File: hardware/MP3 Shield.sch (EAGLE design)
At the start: 62 parts, among them J1 ISP/SPI, Q1 12.288MHz, U1 3.3V, U2 ARDUINO_R3_SHIELD, U3 VS1053, U4 1.8V, U6 USD-SOCKET, U7 74HC4050 LVL CONVERTER

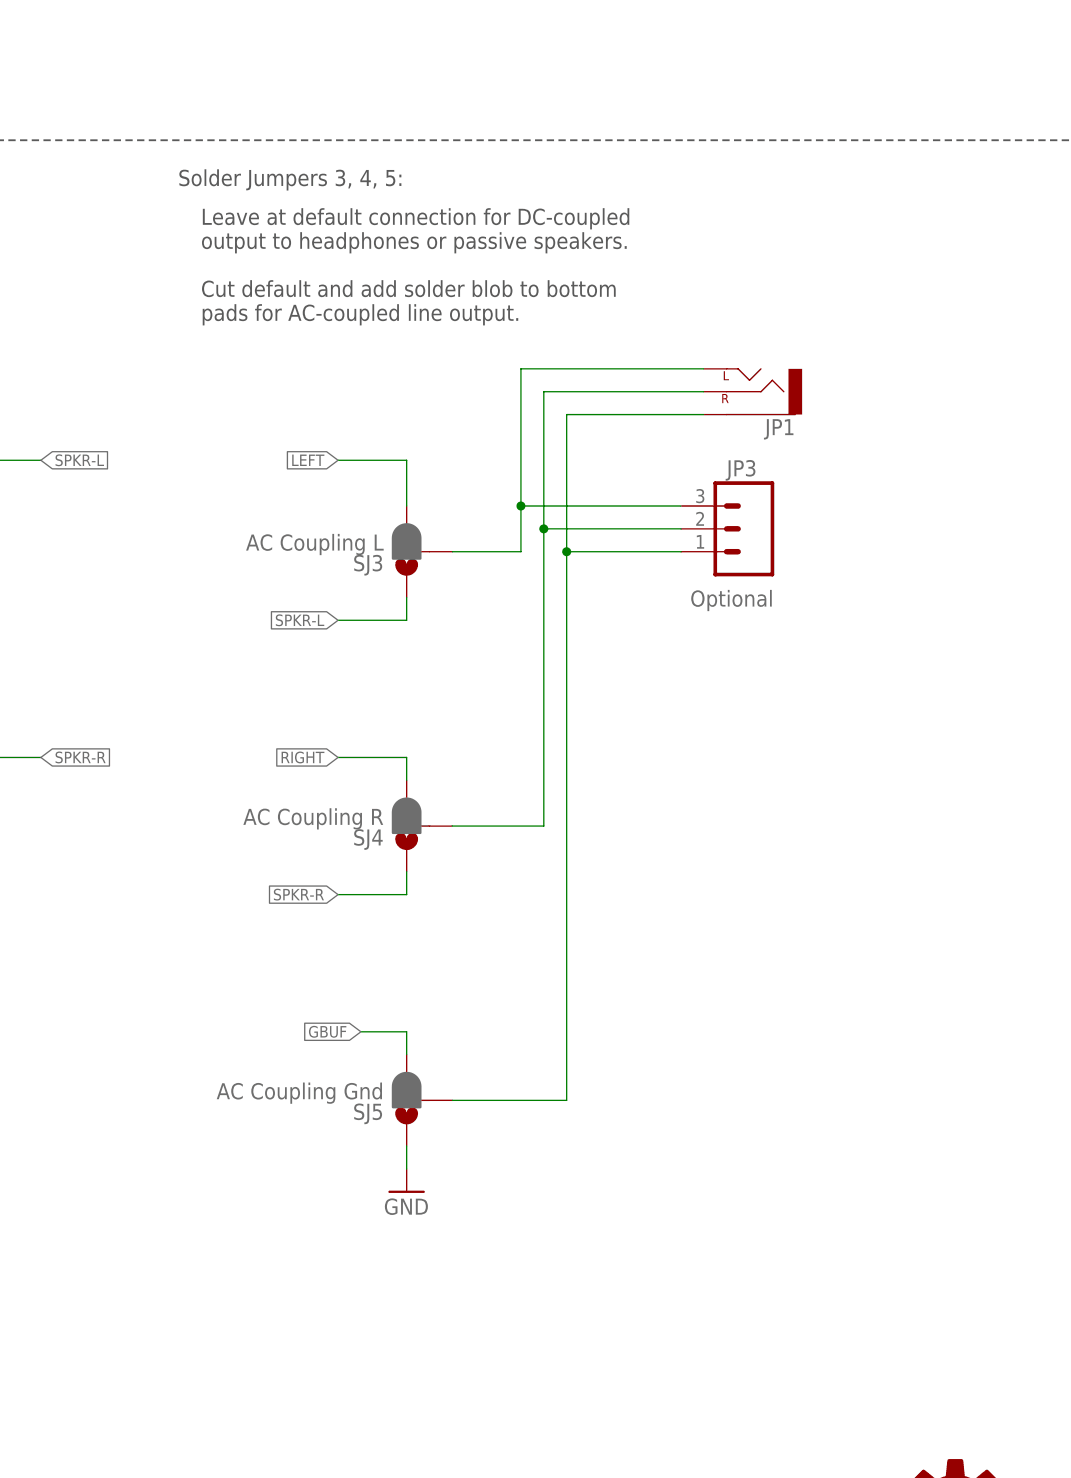
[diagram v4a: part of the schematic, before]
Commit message: Tweaking after review
Clarifying solder jumpers for output configuration.
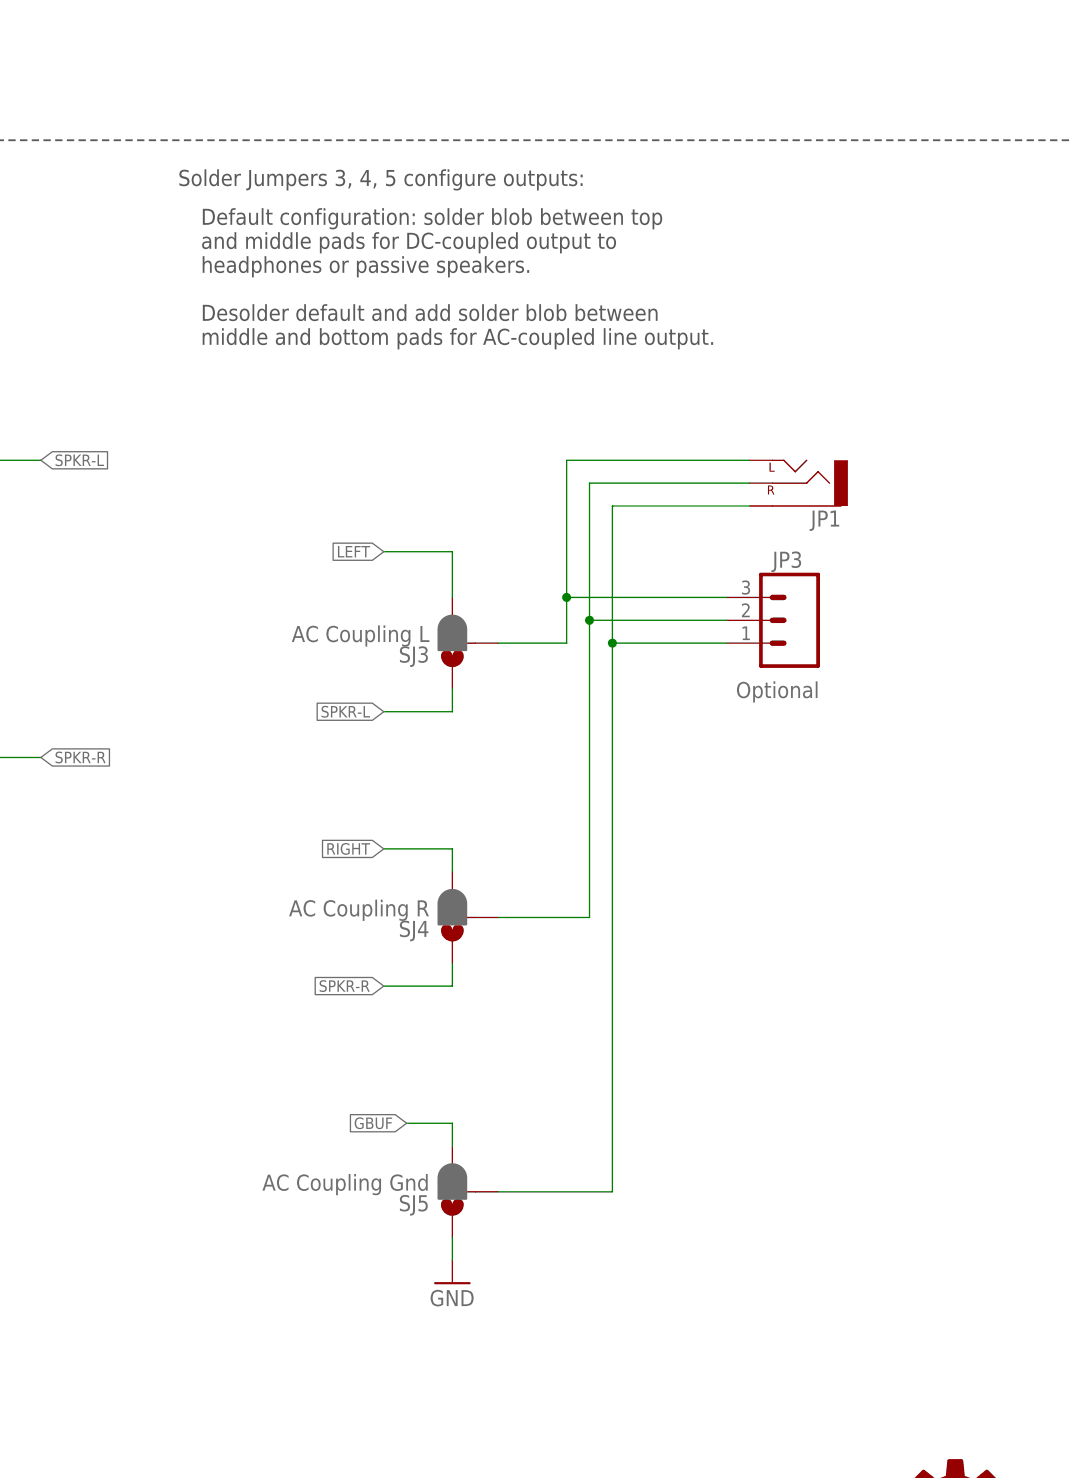
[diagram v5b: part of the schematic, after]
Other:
- note added: "Default configuration: solder blob between top and middle pads for DC-coupled output to headphones or passive speakers. Desolder default and add solder blob between middle and bottom pads for AC-coupled line output."
- note added: "Solder Jumpers 3, 4, 5 configure outputs:"
- note removed: "Leave at default connection for DC-coupled output to headphones or passive speakers. Cut default and add solder blob to bottom pads for AC-coupled line output."
- note removed: "Solder Jumpers 3, 4, 5:"
- moved on the sheet: JP1, JP3, SJ3, SJ4, SJ5
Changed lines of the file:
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@@
 <text x="325.12" y="256.54" size="1.778" layer="97">New on v1.4:</text>
 <text x="327.66" y="254" size="1.778" layer="97">Added solder jumper to select between GBUF and GND</text>
-<text x="332.74" y="190.5" size="1.778" layer="97" align="top-left">Leave at default connection for DC-coupled
-output to headphones or passive speakers.
-Cut default and add solder blob to bottom
-pads for AC-coupled line output.</text>
+<text x="332.74" y="190.5" size="1.778" layer="97" align="top-left">Default configuration: solder blob between top
+and middle pads for DC-coupled output to
+headphones or passive speakers.
+Desolder default and add solder blob between
+middle and bottom pads for AC-coupled line output.</text>
 <text x="327.66" y="251.46" size="1.778" layer="97">Update to Arduino R3 shield type</text>
 <text x="327.66" y="248.92" size="1.778" layer="97">Updated version code</text>
@@
 <text x="327.66" y="241.3" size="1.778" layer="97">Added transient free line-out connection</text>
 <text x="327.66" y="238.76" size="1.778" layer="97">Added MUTE</text>
-<text x="330.2" y="193.04" size="1.778" layer="97">Solder Jumpers 3, 4, 5:</text>
+<text x="330.2" y="193.04" size="1.778" layer="97">Solder Jumpers 3, 4, 5 configure outputs:</text>
 <text x="15.24" y="243.84" size="1.778" layer="97">150mA</text>
 <text x="15.24" y="210.82" size="1.778" layer="97">150mA</text>
@@
 <instance part="TP2" gate="G$1" x="66.04" y="231.14"/>
 <instance part="R13" gate="G$1" x="172.72" y="58.42"/>
-<instance part="JP1" gate="G$1" x="393.7" y="170.18" rot="R180"/>
+<instance part="JP1" gate="G$1" x="398.78" y="160.02" rot="R180"/>
 <instance part="SJ2" gate="1" x="160.02" y="58.42" smashed="yes">
 <attribute name="NAME" x="155.448" y="54.61" size="1.778" layer="95"/>
 <attribute name="VALUE" x="161.544" y="54.61" size="1.778" layer="96"/>
 </instance>
-<instance part="JP3" gate="G$1" x="393.7" y="154.94" smashed="yes" rot="MR0">
-<attribute name="NAME" x="391.16" y="160.782" size="1.778" layer="95"/>
-<attribute name="VALUE" x="387.096" y="146.304" size="1.778" layer="96"/>
+<instance part="JP3" gate="G$1" x="398.78" y="144.78" smashed="yes" rot="MR0">
+<attribute name="NAME" x="396.24" y="150.622" size="1.778" layer="95"/>
+<attribute name="VALUE" x="392.176" y="136.144" size="1.778" layer="96"/>
 </instance>
 <instance part="U6" gate="G$1" x="215.9" y="246.38"/>
@@
 <instance part="P+9" gate="1" x="60.96" y="109.22"/>
 <instance part="U$1" gate="G$1" x="331.47" y="6.858"/>
-<instance part="SJ3" gate="G$1" x="355.6" y="152.4" rot="R180"/>
-<instance part="SJ4" gate="G$1" x="355.6" y="121.92" rot="R180"/>
-<instance part="SJ5" gate="G$1" x="355.6" y="91.44" rot="R180"/>
-<instance part="GND29" gate="1" x="355.6" y="81.28"/>
+<instance part="SJ3" gate="G$1" x="360.68" y="142.24" rot="R180"/>
+<instance part="SJ4" gate="G$1" x="360.68" y="111.76" rot="R180"/>
+<instance part="SJ5" gate="G$1" x="360.68" y="81.28" rot="R180"/>
+<instance part="GND29" gate="1" x="360.68" y="71.12"/>
 </instances>
 <busses>
@@
 <pinref part="GND29" gate="1" pin="GND"/>
 <pinref part="SJ5" gate="G$1" pin="1"/>
-<wire x1="355.6" y1="83.82" x2="355.6" y2="86.36" width="0.1524" layer="91"/>
+<wire x1="360.68" y1="73.66" x2="360.68" y2="76.2" width="0.1524" layer="91"/>
 </segment>
 </net>
@@
 </segment>
 <segment>
-<label x="347.98" y="162.56" size="1.27" layer="95" rot="R180" xref="yes"/>
+<label x="353.06" y="152.4" size="1.27" layer="95" rot="R180" xref="yes"/>
 <pinref part="SJ3" gate="G$1" pin="3"/>
-<wire x1="355.6" y1="157.48" x2="355.6" y2="162.56" width="0.1524" layer="91"/>
-<wire x1="355.6" y1="162.56" x2="347.98" y2="162.56" width="0.1524" layer="91"/>
+<wire x1="360.68" y1="147.32" x2="360.68" y2="152.4" width="0.1524" layer="91"/>
+<wire x1="360.68" y1="152.4" x2="353.06" y2="152.4" width="0.1524" layer="91"/>
 </segment>
 </net>
@@
 </segment>
 <segment>
-<label x="347.98" y="129.54" size="1.27" layer="95" rot="R180" xref="yes"/>
+<label x="353.06" y="119.38" size="1.27" layer="95" rot="R180" xref="yes"/>
 <pinref part="SJ4" gate="G$1" pin="3"/>
-<wire x1="355.6" y1="127" x2="355.6" y2="129.54" width="0.1524" layer="91"/>
-<wire x1="355.6" y1="129.54" x2="347.98" y2="129.54" width="0.1524" layer="91"/>
+<wire x1="360.68" y1="116.84" x2="360.68" y2="119.38" width="0.1524" layer="91"/>
+<wire x1="360.68" y1="119.38" x2="353.06" y2="119.38" width="0.1524" layer="91"/>
 </segment>
 </net>
@@
 </segment>
 <segment>
-<label x="350.52" y="99.06" size="1.27" layer="95" rot="R180" xref="yes"/>
-<wire x1="350.52" y1="99.06" x2="355.6" y2="99.06" width="0.1524" layer="91"/>
+<label x="355.6" y="88.9" size="1.27" layer="95" rot="R180" xref="yes"/>
+<wire x1="355.6" y1="88.9" x2="360.68" y2="88.9" width="0.1524" layer="91"/>
 <pinref part="SJ5" gate="G$1" pin="3"/>
-<wire x1="355.6" y1="99.06" x2="355.6" y2="96.52" width="0.1524" layer="91"/>
+<wire x1="360.68" y1="88.9" x2="360.68" y2="86.36" width="0.1524" layer="91"/>
 </segment>
 </net>
@@
 </segment>
 <segment>
-<label x="347.98" y="114.3" size="1.27" layer="95" rot="R180" xref="yes"/>
-<wire x1="347.98" y1="114.3" x2="355.6" y2="114.3" width="0.1524" layer="91"/>
-<wire x1="355.6" y1="114.3" x2="355.6" y2="116.84" width="0.1524" layer="91"/>
+<label x="353.06" y="104.14" size="1.27" layer="95" rot="R180" xref="yes"/>
+<wire x1="353.06" y1="104.14" x2="360.68" y2="104.14" width="0.1524" layer="91"/>
+<wire x1="360.68" y1="104.14" x2="360.68" y2="106.68" width="0.1524" layer="91"/>
 <pinref part="SJ4" gate="G$1" pin="1"/>
 </segment>
@@
 </segment>
 <segment>
-<label x="347.98" y="144.78" size="1.27" layer="95" rot="R180" xref="yes"/>
+<label x="353.06" y="134.62" size="1.27" layer="95" rot="R180" xref="yes"/>
 <pinref part="SJ3" gate="G$1" pin="1"/>
-<wire x1="355.6" y1="147.32" x2="355.6" y2="144.78" width="0.1524" layer="91"/>
-<wire x1="355.6" y1="144.78" x2="347.98" y2="144.78" width="0.1524" layer="91"/>
+<wire x1="360.68" y1="137.16" x2="360.68" y2="134.62" width="0.1524" layer="91"/>
+<wire x1="360.68" y1="134.62" x2="353.06" y2="134.62" width="0.1524" layer="91"/>
 </segment>
 </net>
@@
 <segment>
 <pinref part="SJ5" gate="G$1" pin="2"/>
-<wire x1="360.68" y1="91.44" x2="373.38" y2="91.44" width="0.1524" layer="91"/>
-<wire x1="373.38" y1="91.44" x2="373.38" y2="152.4" width="0.1524" layer="91"/>
+<wire x1="365.76" y1="81.28" x2="378.46" y2="81.28" width="0.1524" layer="91"/>
+<wire x1="378.46" y1="81.28" x2="378.46" y2="142.24" width="0.1524" layer="91"/>
 <pinref part="JP1" gate="G$1" pin="SLEEVE"/>
-<wire x1="373.38" y1="152.4" x2="373.38" y2="167.64" width="0.1524" layer="91"/>
-<wire x1="373.38" y1="167.64" x2="388.62" y2="167.64" width="0.1524" layer="91"/>
+<wire x1="378.46" y1="142.24" x2="378.46" y2="157.48" width="0.1524" layer="91"/>
+<wire x1="378.46" y1="157.48" x2="393.7" y2="157.48" width="0.1524" layer="91"/>
 <pinref part="JP3" gate="G$1" pin="1"/>
-<wire x1="386.08" y1="152.4" x2="373.38" y2="152.4" width="0.1524" layer="91"/>
-<junction x="373.38" y="152.4"/>
+<wire x1="391.16" y1="142.24" x2="378.46" y2="142.24" width="0.1524" layer="91"/>
+<junction x="378.46" y="142.24"/>
 </segment>
 </net>
@@
 <segment>
 <pinref part="SJ4" gate="G$1" pin="2"/>
-<wire x1="360.68" y1="121.92" x2="370.84" y2="121.92" width="0.1524" layer="91"/>
-<wire x1="370.84" y1="121.92" x2="370.84" y2="154.94" width="0.1524" layer="91"/>
+<wire x1="365.76" y1="111.76" x2="375.92" y2="111.76" width="0.1524" layer="91"/>
+<wire x1="375.92" y1="111.76" x2="375.92" y2="144.78" width="0.1524" layer="91"/>
 <pinref part="JP1" gate="G$1" pin="RIGHT"/>
-<wire x1="370.84" y1="154.94" x2="370.84" y2="170.18" width="0.1524" layer="91"/>
-<wire x1="370.84" y1="170.18" x2="388.62" y2="170.18" width="0.1524" layer="91"/>
+<wire x1="375.92" y1="144.78" x2="375.92" y2="160.02" width="0.1524" layer="91"/>
+<wire x1="375.92" y1="160.02" x2="393.7" y2="160.02" width="0.1524" layer="91"/>
 <pinref part="JP3" gate="G$1" pin="2"/>
-<wire x1="386.08" y1="154.94" x2="370.84" y2="154.94" width="0.1524" layer="91"/>
-<junction x="370.84" y="154.94"/>
+<wire x1="391.16" y1="144.78" x2="375.92" y2="144.78" width="0.1524" layer="91"/>
+<junction x="375.92" y="144.78"/>
 </segment>
 </net>
@@
 <segment>
 <pinref part="SJ3" gate="G$1" pin="2"/>
-<wire x1="360.68" y1="152.4" x2="368.3" y2="152.4" width="0.1524" layer="91"/>
-<wire x1="368.3" y1="152.4" x2="368.3" y2="157.48" width="0.1524" layer="91"/>
+<wire x1="365.76" y1="142.24" x2="373.38" y2="142.24" width="0.1524" layer="91"/>
+<wire x1="373.38" y1="142.24" x2="373.38" y2="147.32" width="0.1524" layer="91"/>
 <pinref part="JP1" gate="G$1" pin="LEFT"/>
-<wire x1="368.3" y1="157.48" x2="368.3" y2="172.72" width="0.1524" layer="91"/>
-<wire x1="368.3" y1="172.72" x2="388.62" y2="172.72" width="0.1524" layer="91"/>
+<wire x1="373.38" y1="147.32" x2="373.38" y2="162.56" width="0.1524" layer="91"/>
+<wire x1="373.38" y1="162.56" x2="393.7" y2="162.56" width="0.1524" layer="91"/>
 <pinref part="JP3" gate="G$1" pin="3"/>
-<wire x1="386.08" y1="157.48" x2="368.3" y2="157.48" width="0.1524" layer="91"/>
-<junction x="368.3" y="157.48"/>
-</segment>
-</net>
+<wire x1="391.16" y1="147.32" x2="373.38" y2="147.32" width="0.1524" layer="91"/>
+<junction x="373.38" y="147.32"/>
+</segment>
+</net>

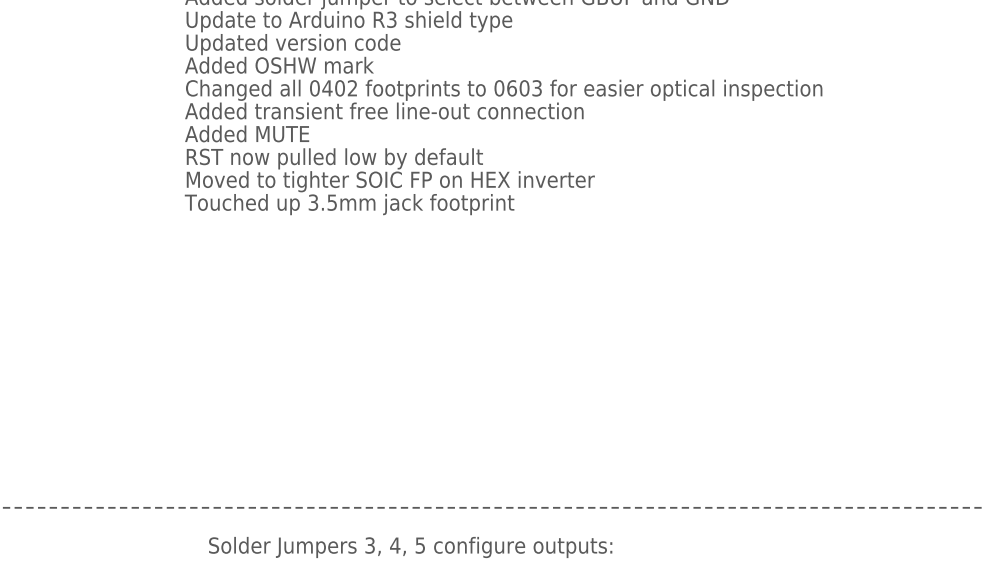
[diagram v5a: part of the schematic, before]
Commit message: Updating based on QC checklist.
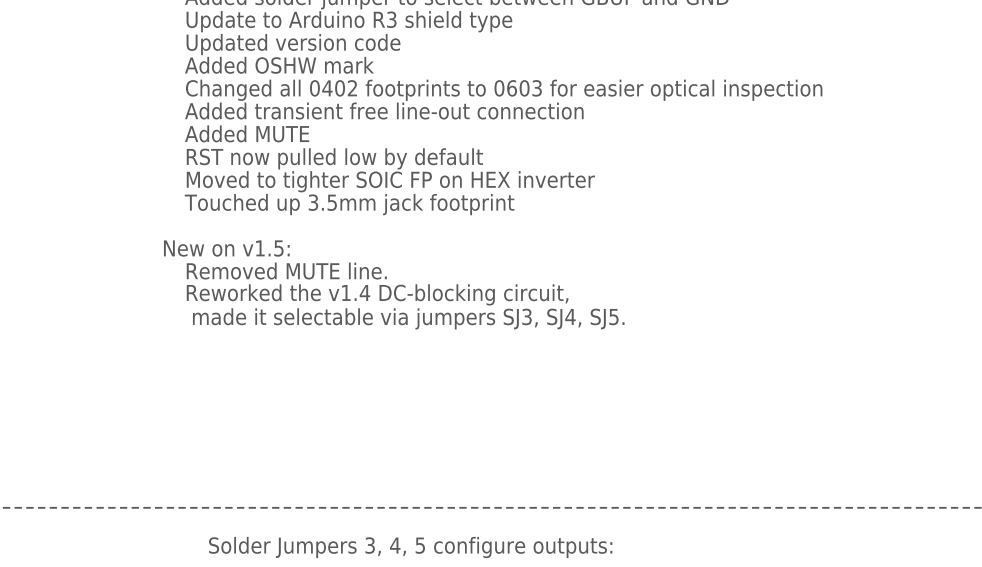
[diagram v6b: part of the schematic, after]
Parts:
- Q1: PROD_ID (none) -> XTAL-09653
- U6: PROD_ID (none) -> CONN-07820
- U7: PROD_ID (none) -> IC-09604
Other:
- note added: "New on v1.5:"
- note added: "Removed MUTE line."
- note added: "Reworked the v1.4 DC-blocking circuit, made it selectable via jumpers SJ3, SJ4, SJ5."
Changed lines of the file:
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@@
 <part name="C3" library="SparkFun-Capacitors" deviceset="22PF-50V-5%(0603)" device="" value="22pF"/>
 <part name="C8" library="SparkFun-Capacitors" deviceset="22PF-50V-5%(0603)" device="" value="22pF"/>
-<part name="Q1" library="SparkFun" deviceset="CRYSTAL" device="5X3" value="12.288MHz"/>
+<part name="Q1" library="SparkFun" deviceset="CRYSTAL" device="5X3" value="12.288MHz">
+<attribute name="PROD_ID" value="XTAL-09653"/>
+</part>
 <part name="R1" library="SparkFun-Resistors" deviceset="1M-1%" device="" value="1M"/>
 <part name="C9" library="SparkFun-Capacitors" deviceset="1.0UF-16V-10%(0603)" device="" value="1.0uF"/>
@@
 <part name="SJ2" library="SparkFun" deviceset="SOLDERJUMPER" device="TRACE" value="NC"/>
 <part name="JP3" library="SparkFun" deviceset="M03" device="PTH" value="Optional"/>
-<part name="U6" library="SparkFun" deviceset="USD-SOCKET" device="NEW" value="USD-SOCKET"/>
+<part name="U6" library="SparkFun" deviceset="USD-SOCKET" device="NEW" value="USD-SOCKET">
+<attribute name="PROD_ID" value="CONN-07820"/>
+</part>
 <part name="P+10" library="SparkFun" deviceset="3.3V" device=""/>
 <part name="GND16" library="SparkFun" deviceset="GND" device=""/>
-<part name="U7" library="SparkFun-DigitalIC" deviceset="HEX_CONVERTER" device="" value="74HC4050 LVL CONVERTER"/>
+<part name="U7" library="SparkFun-DigitalIC" deviceset="HEX_CONVERTER" device="" value="74HC4050 LVL CONVERTER">
+<attribute name="PROD_ID" value="IC-09604"/>
+</part>
 <part name="P+11" library="SparkFun" deviceset="3.3V" device=""/>
 <part name="GND25" library="SparkFun" deviceset="GND" device=""/>
@@
 <text x="327.66" y="231.14" size="1.778" layer="97">Touched up 3.5mm jack footprint</text>
 <text x="357.886" y="6.604" size="1.778" layer="97">Byron Jacquot</text>
+<text x="325.12" y="226.06" size="1.778" layer="97">New on v1.5:</text>
+<text x="327.66" y="223.52" size="1.778" layer="97">Removed MUTE line.</text>
+<text x="327.66" y="218.44" size="1.778" layer="97">Reworked the v1.4 DC-blocking circuit,
+ made it selectable via jumpers SJ3, SJ4, SJ5.</text>
 </plain>
 <instances>
@@
 <instance part="C3" gate="G$1" x="53.34" y="149.86" rot="R90"/>
 <instance part="C8" gate="G$1" x="53.34" y="134.62" rot="R90"/>
-<instance part="Q1" gate="G$1" x="58.42" y="142.24" rot="R90"/>
+<instance part="Q1" gate="G$1" x="58.42" y="142.24" rot="R90">
+<attribute name="PROD_ID" x="58.42" y="142.24" size="1.778" layer="96" rot="R90" display="off"/>
+</instance>
 <instance part="R1" gate="G$1" x="63.5" y="142.24" rot="R90"/>
 <instance part="C9" gate="G$1" x="154.94" y="139.7" smashed="yes" rot="R180">
@@
 <attribute name="VALUE" x="392.176" y="136.144" size="1.778" layer="96"/>
 </instance>
-<instance part="U6" gate="G$1" x="215.9" y="246.38"/>
+<instance part="U6" gate="G$1" x="215.9" y="246.38">
+<attribute name="PROD_ID" x="215.9" y="246.38" size="1.778" layer="96" display="off"/>
+</instance>
 <instance part="P+10" gate="G$1" x="205.74" y="261.62"/>
 <instance part="GND16" gate="1" x="205.74" y="223.52"/>
@@
 <attribute name="NAME" x="155.194" y="259.588" size="1.778" layer="95"/>
 <attribute name="VALUE" x="134.112" y="236.22" size="1.778" layer="95"/>
+<attribute name="PROD_ID" x="162.56" y="248.92" size="1.778" layer="96" display="off"/>
 </instance>
 <instance part="P+11" gate="G$1" x="149.86" y="259.08"/>
